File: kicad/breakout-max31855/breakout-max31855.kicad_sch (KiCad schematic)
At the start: 19 parts, among them U1 MAX31855K

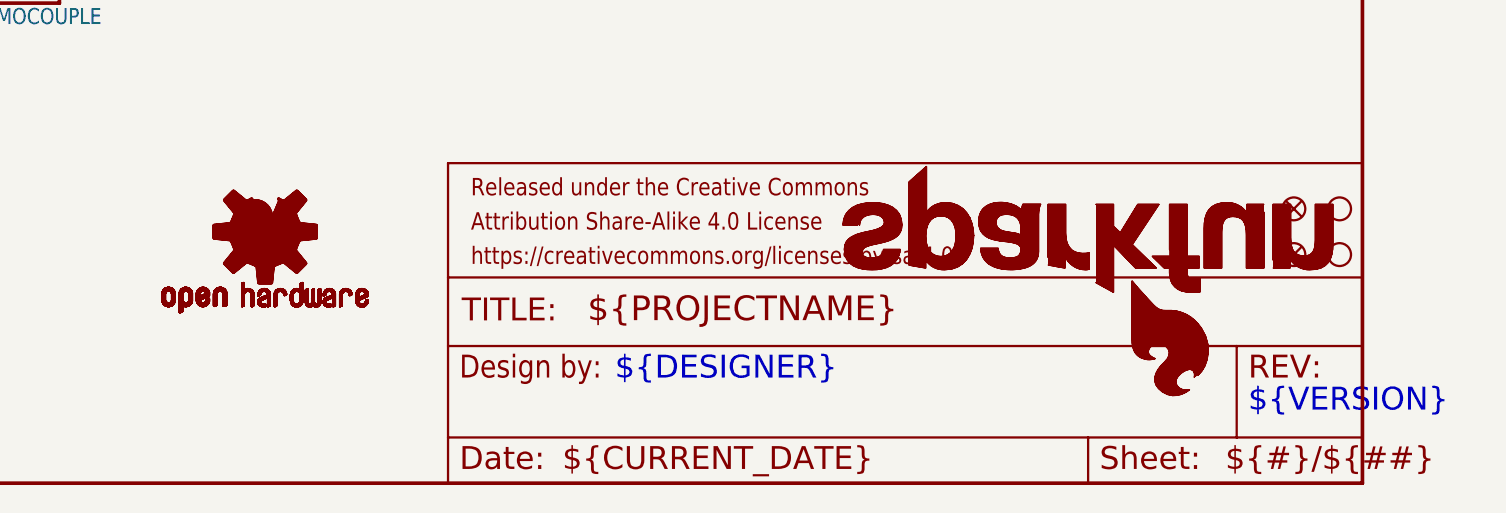
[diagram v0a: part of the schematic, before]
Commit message: Prune unused eagle-import symbols from breakout schematic cache
KiCad auto-pruned the embedded (lib_symbols ...) block in
breakout-max31855.kicad_sch on first open — down from 39,614 lines
(every symbol in SparkFun's Eagle library, cached by the importer) to
just the ~15 symbols actually placed on the sheet. File shrinks from
717 KB to ~50 KB, no functional change.

Also mirrors sch_revision "1.0-draft" from the title_block into
.kicad_pro's ipc2581 metadata section (KiCad normal housekeeping on
project open).

Co-Authored-By: Claude Opus 4.7 (1M context) <noreply@anthropic.com>
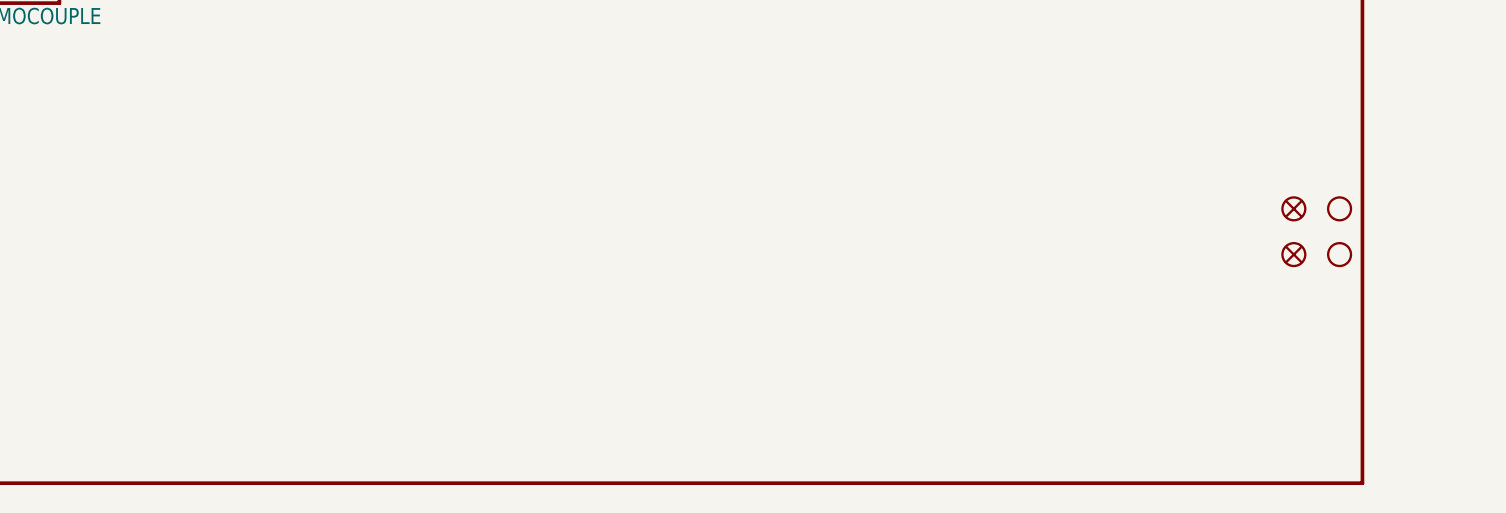
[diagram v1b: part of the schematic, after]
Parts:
- removed unit 2 of FRAME1
- removed LOGO1, LOGO4: OSHW-LOGOS, SparkFun_Thermocouple_Breakout:OSHW-LOGO-S, symbol SparkFun_Thermocouple_Breakout-eagle-import:OSHW-LOGOS
- removed LOGO2, LOGO3: SFE_LOGO_NAME_FLAME.1_INCH, SparkFun_Thermocouple_Breakout:SFE_LOGO_NAME_FLAME_.1, symbol SparkFun_Thermocouple_Breakout-eagle-import:SFE_LOGO_NAME_FLAME.1_INCH
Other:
- note removed: "${DESIGNER}"
- note removed: "${VERSION}"

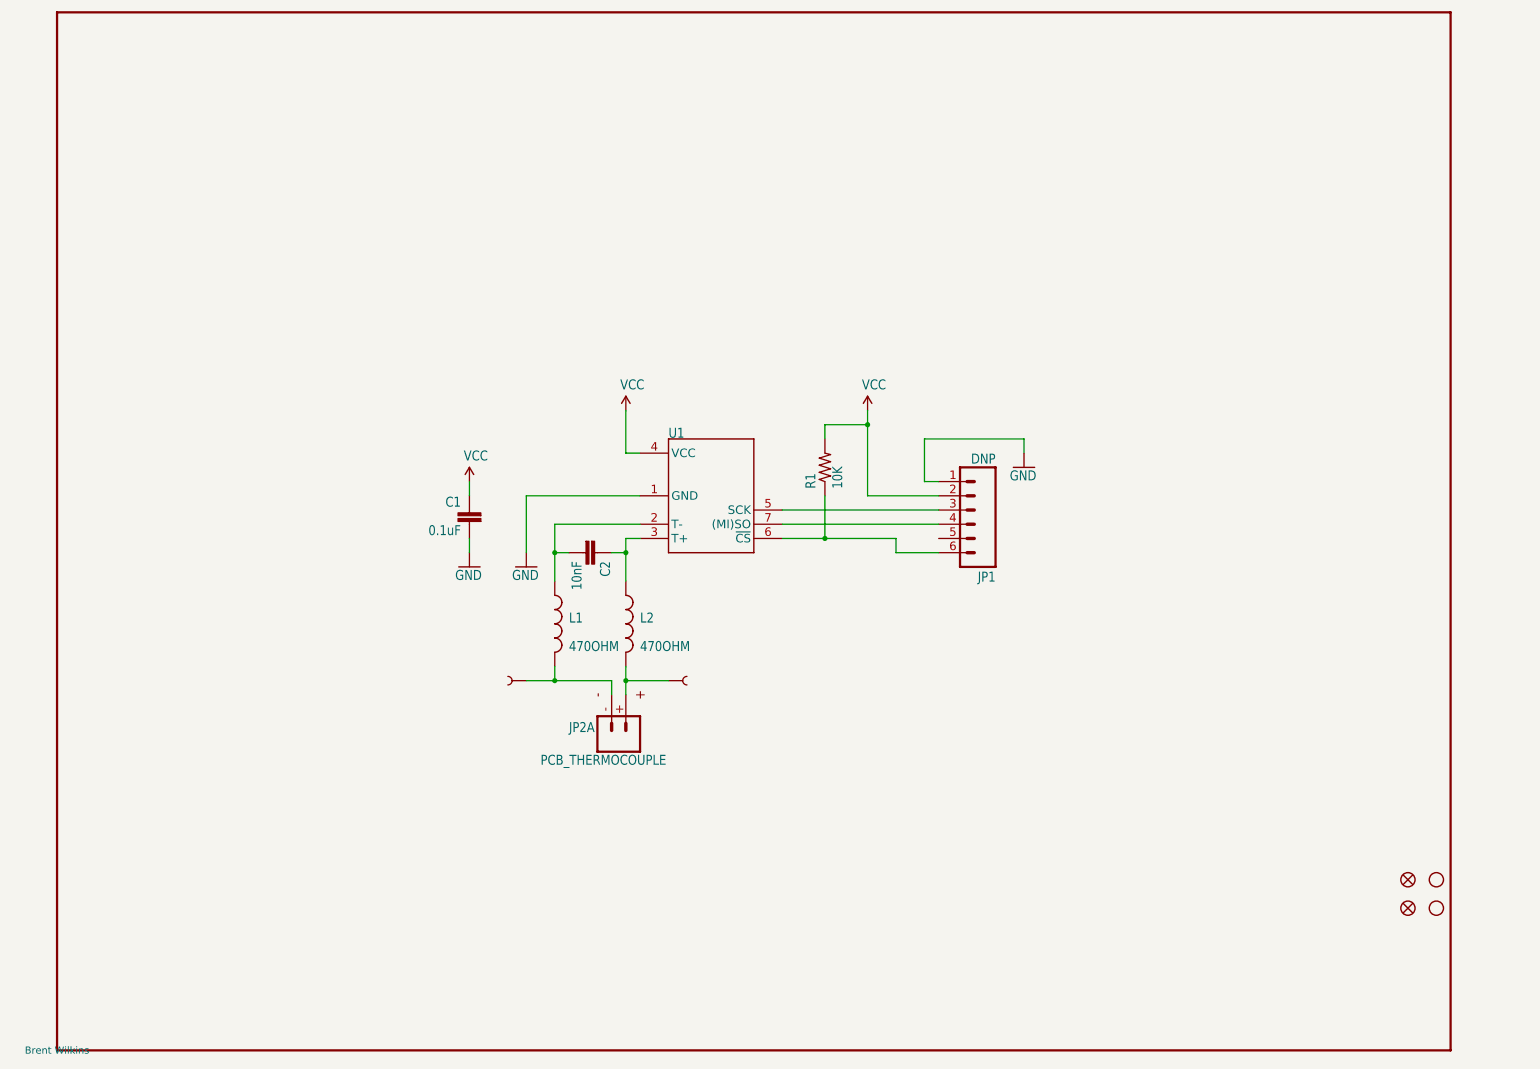
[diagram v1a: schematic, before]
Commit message: Session 4: fresh-draw schematic + BOM sourcing for MD-TC-BRK v1.0
Replaces the Eagle-imported content with a hand-drawn schematic built on KiCad 10
stock symbols. Cleaner visual, reviewer-friendly, matches the v1 board's convention.

- Delete Eagle-imported artefacts: .kicad_pcb, -eagle-import.kicad_sym, sym-lib-table
- Rewrite breakout-max31855.kicad_sch with 15 placed components (U1, C1-C4, CY1,
  FB1, R1, RB1, D1, J1, JP1, MH1, SJ1, TP1) + 4 power/flag symbols
- Assign footprints, set DNP flags on C3/C4/D1/CY1
- Add Manufacturer, MPN, Supplier, Supplier_PN properties to 12 orderable components
  for direct BOM export to DigiKey/Mantech
- Power net renamed VCC -> +3V3 (voltage-explicit, prevents 3V3-vs-5V mis-wiring
  on stripboard where both rails are present; MAX31855 Vmax is 3.6V)
- New schematic-guide.md: component table, net list, draw order, ERC checklist,
  BOM export commands

Not yet done: add FB2/D2/TP2, wire the schematic, run ERC to zero.

Co-Authored-By: Claude Opus 4.7 (1M context) <noreply@anthropic.com>
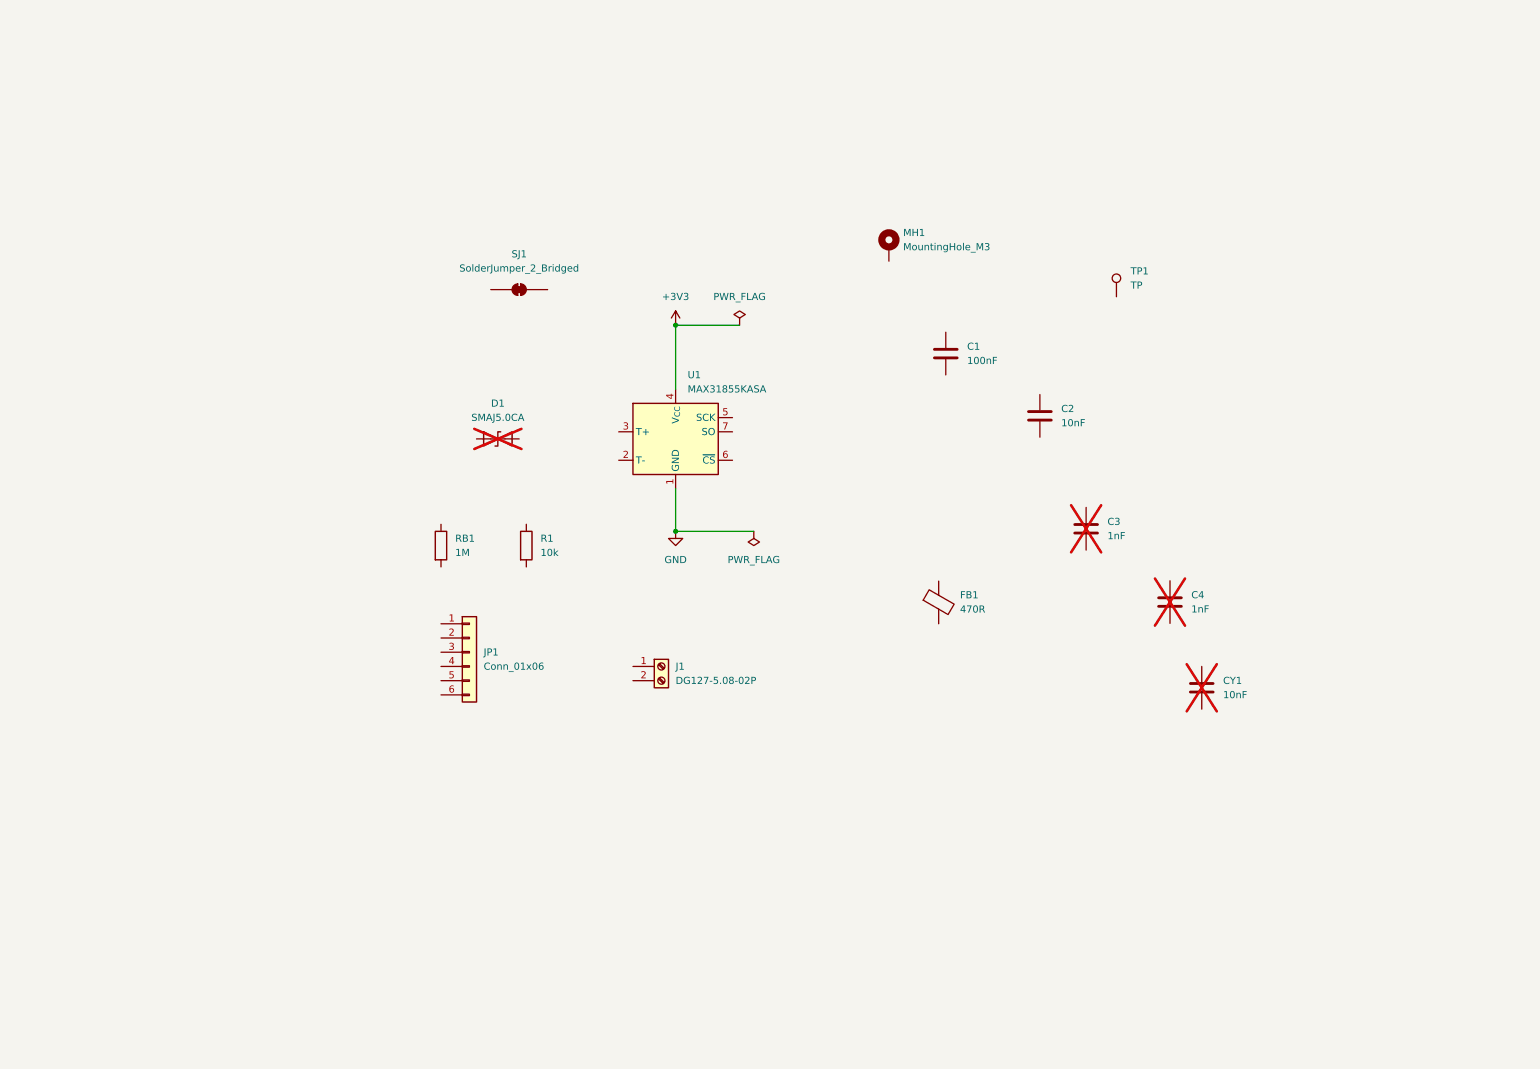
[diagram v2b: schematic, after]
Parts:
- removed C1: 0.1uF, SparkFun_Thermocouple_Breakout:0603-CAP, symbol SparkFun_Thermocouple_Breakout-eagle-import:0.1UF-25V(+80/-20%)(0603)
- removed C2: 10nF, SparkFun_Thermocouple_Breakout:0603-CAP, symbol SparkFun_Thermocouple_Breakout-eagle-import:10NF/10000PF-50V-10%(0603)
- removed FID1, FID2: FIDUCIAL1X2, SparkFun_Thermocouple_Breakout:FIDUCIAL-1X2, symbol SparkFun_Thermocouple_Breakout-eagle-import:FIDUCIAL1X2
- removed FRAME1: >VERSION, SparkFun_Thermocouple_Breakout:CREATIVE_COMMONS, symbol SparkFun_Thermocouple_Breakout-eagle-import:FRAME-LETTER
- removed JP1: DNP, SparkFun_Thermocouple_Breakout:1X06, symbol SparkFun_Thermocouple_Breakout-eagle-import:M06SILK_FEMALE_PTH
- removed JP2: PCB_THERMOCOUPLE, SparkFun_Thermocouple_Breakout:PCC-SMP, symbol SparkFun_Thermocouple_Breakout-eagle-import:PCB_THERMOCOUPLE
- removed L1, L2: 470OHM, SparkFun_Thermocouple_Breakout:0603, symbol SparkFun_Thermocouple_Breakout-eagle-import:INDUCTOR0603
- removed R1: 10K, SparkFun_Thermocouple_Breakout:0603-RES, symbol SparkFun_Thermocouple_Breakout-eagle-import:10KOHM-1/10W-1%(0603)0603
- removed STANDOFF1, STANDOFF4: STAND-OFF, SparkFun_Thermocouple_Breakout:STAND-OFF, symbol SparkFun_Thermocouple_Breakout-eagle-import:STAND-OFF
- removed TP1, TP2: TEST-POINTTP_15TH_THRU, SparkFun_Thermocouple_Breakout:TP_15TH, symbol SparkFun_Thermocouple_Breakout-eagle-import:TEST-POINTTP_15TH_THRU
- removed U1: MAX31855K, SparkFun_Thermocouple_Breakout:SOIC8, symbol SparkFun_Thermocouple_Breakout-eagle-import:MAX31855K
- added C1: 100nF, Capacitor_SMD:C_0805_2012Metric, symbol Device:C
- added C2, CY1: 10nF, Capacitor_SMD:C_0805_2012Metric, symbol Device:C
- added C3, C4: 1nF, Capacitor_SMD:C_0805_2012Metric, symbol Device:C
- added D1: SMAJ5.0CA, Diode_SMD:D_SMA, symbol Device:D_TVS
- added FB1: 470R, Inductor_SMD:L_0805_2012Metric, symbol Device:FerriteBead
- added J1: DG127-5.08-02P, Connector_Phoenix_MSTB:PhoenixContact_MSTBA_2,5_2-G-5,08_1x02_P5.08mm_Horizontal, symbol Connector:Screw_Terminal_01x02
- added JP1: Conn_01x06, Connector_PinHeader_2.54mm:PinHeader_1x06_P2.54mm_Vertical, symbol Connector_Generic:Conn_01x06
- added MH1: MountingHole_M3, MountingHole:MountingHole_3.2mm_M3_Pad, symbol Mechanical:MountingHole_Pad_MP
- added R1: 10k, Resistor_SMD:R_0805_2012Metric, symbol Device:R
- added RB1: 1M, Resistor_SMD:R_0805_2012Metric, symbol Device:R
- added SJ1: SolderJumper_2_Bridged, Jumper:SolderJumper-2_P1.3mm_Bridged_RoundedPad1.0x1.5mm, symbol Jumper:SolderJumper_2_Bridged
- added TP1: TP, TestPoint:TestPoint_Pad_D1.5mm, symbol Connector:TestPoint
- added U1: MAX31855KASA, Package_SO:SOIC-8_3.9x4.9mm_P1.27mm, symbol Sensor_Temperature:MAX31855KASA
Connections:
- net GND: now also U1.1 (GND)
- new net +3V3: U1.4 (V_{CC})
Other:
- company: Precept Systems (Pty) Ltd -> (none)
- title: MAX31855K Thermocouple Breakout — MD-TC-BRK v1.0 -> (none)
